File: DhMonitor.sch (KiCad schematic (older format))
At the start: 8 parts, among them J1 ProMiniDTRSide, J2 A4A5, J3 PowerRaw, J4 ProMiniRawSide, J5 RTC, J6 sdCardReader

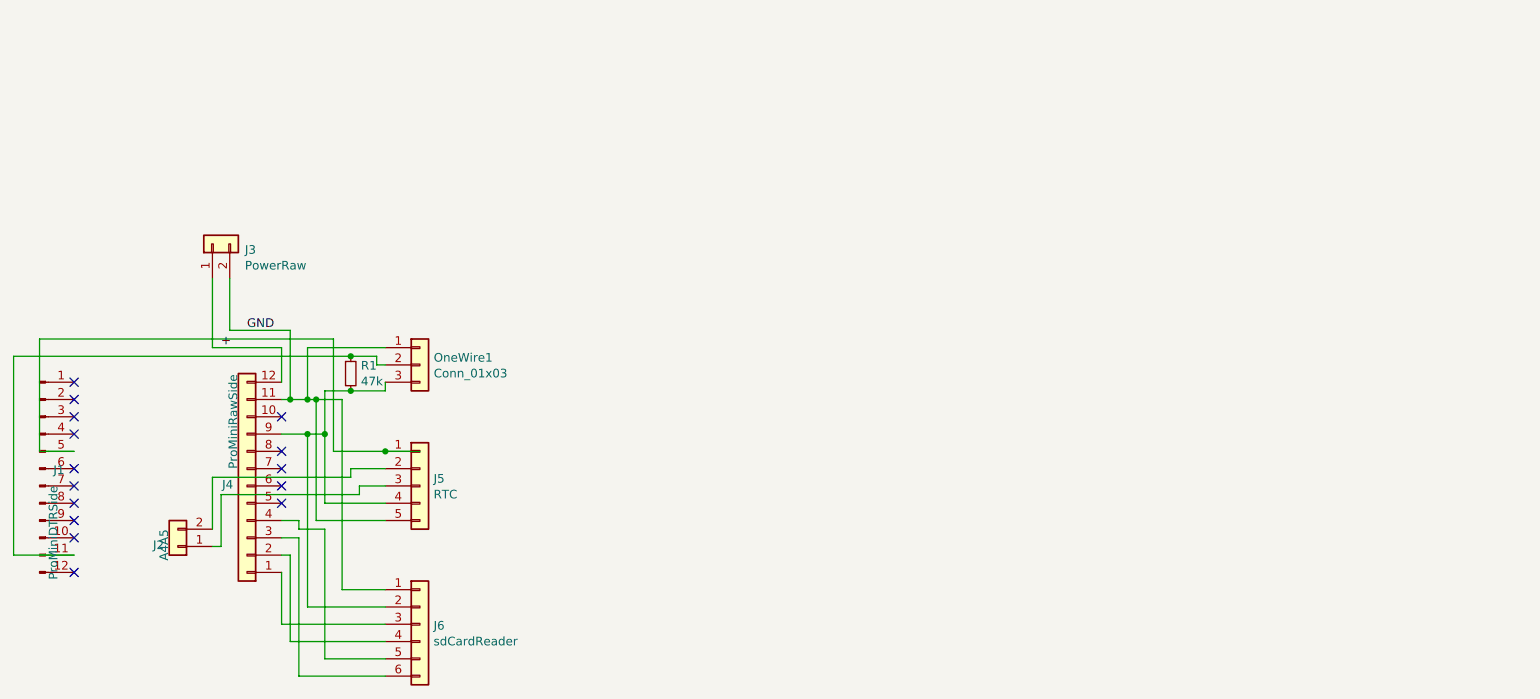
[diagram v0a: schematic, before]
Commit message: solves wrong files :o
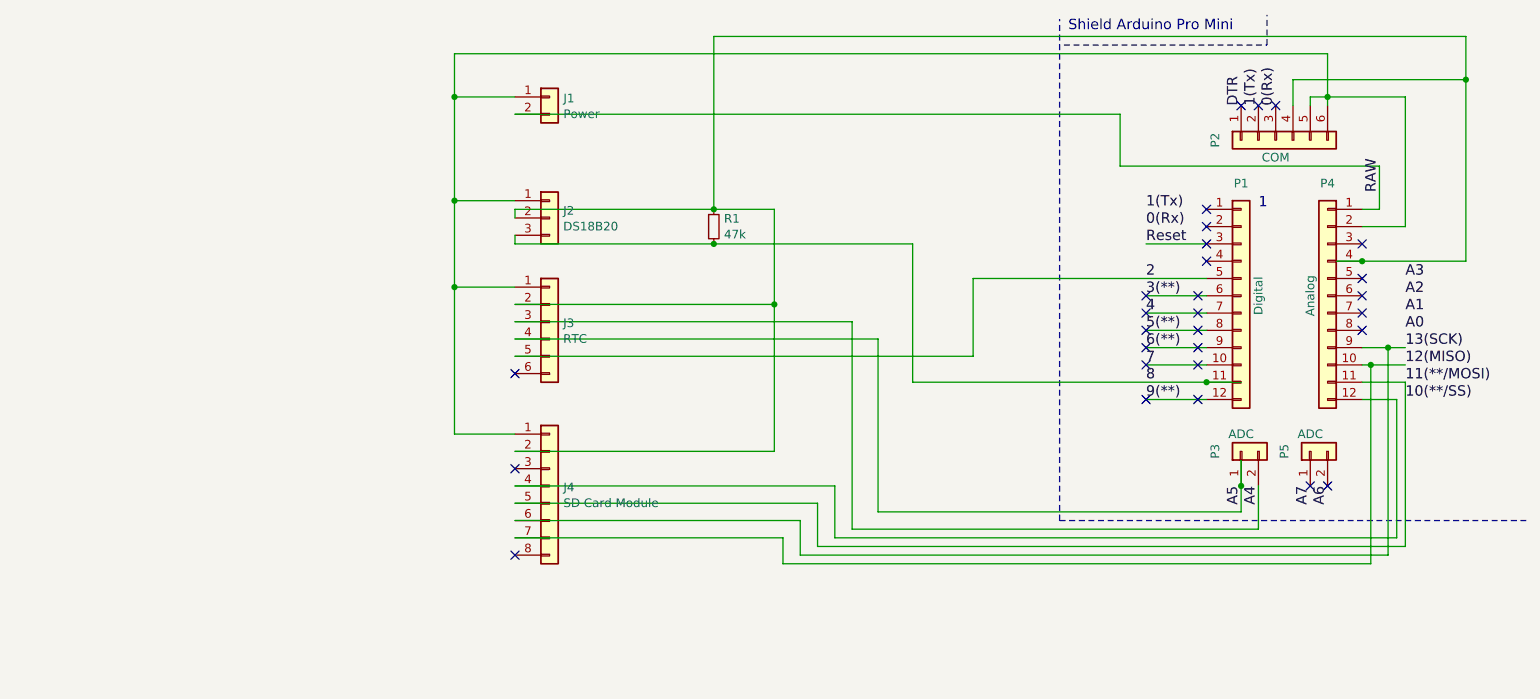
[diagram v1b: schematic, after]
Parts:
- removed J1: ProMiniDTRSide, Connector_PinSocket_2.54mm:PinSocket_1x12_P2.54mm_Vertical, symbol Connector:Conn_01x12_Male
- removed J2: A4A5, Connector_PinHeader_2.54mm:PinHeader_1x02_P2.54mm_Vertical, symbol Connector_Generic:Conn_01x02
- removed J3: PowerRaw, Connector_PinHeader_2.54mm:PinHeader_1x02_P2.54mm_Vertical, symbol Connector_Generic:Conn_01x02
- removed J4: ProMiniRawSide, Connector_PinSocket_2.54mm:PinSocket_1x12_P2.54mm_Vertical, symbol Connector_Generic:Conn_01x12
- removed J5: RTC, Connector_PinHeader_2.54mm:PinHeader_1x05_P2.54mm_Vertical, symbol Connector_Generic:Conn_01x05
- removed J6: sdCardReader, Connector_PinSocket_2.54mm:PinSocket_1x06_P2.54mm_Vertical, symbol Connector_Generic:Conn_01x06
- removed OneWire1: Conn_01x03, Connector_PinSocket_2.54mm:PinSocket_1x03_P2.54mm_Vertical, symbol Connector_Generic:Conn_01x03
- added J1: Power, Connector_PinHeader_2.54mm:PinHeader_1x02_P2.54mm_Horizontal, symbol Connector_Generic:Conn_01x02
- added J2: DS18B20, Connector_PinHeader_2.54mm:PinHeader_1x03_P2.54mm_Vertical, symbol Connector_Generic:Conn_01x03
- added J3: RTC, Connector_PinHeader_2.54mm:PinHeader_1x06_P2.54mm_Vertical, symbol Connector_Generic:Conn_01x06
- added J4: SD Card Module, Connector_PinHeader_2.54mm:PinHeader_1x08_P2.54mm_Vertical, symbol Connector_Generic:Conn_01x08
- added P1: Digital, Socket_Arduino_Pro_Mini:Socket_Strip_Arduino_1x12, symbol Connector_Generic:Conn_01x12
- added P2: COM, Socket_Arduino_Pro_Mini:Socket_Strip_Arduino_1x06, symbol Connector_Generic:Conn_01x06
- added P3, P5: ADC, Socket_Arduino_Pro_Mini:Socket_Strip_Arduino_1x02, symbol Connector_Generic:Conn_01x02
- added P4: Analog, Socket_Arduino_Pro_Mini:Socket_Strip_Arduino_1x12, symbol Connector_Generic:Conn_01x12
- R1: footprint Resistor_THT:R_Axial_DIN0204_L3.6mm_D1.6mm_P2.54mm_Vertical -> OptoDevice:R_LDR_4.9x4.2mm_P2.54mm_Vertical
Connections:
- net labels added: 0(Rx), 1(Tx), 10(**/SS), 11(**/MOSI), 12(MISO), 13(SCK), 2, 3(**), 4, 5(**), 6(**), 7, 8, 9(**), A0, A1, A2, A3, A4, A5, A6, A7, DTR, RAW, Reset
- net labels removed: +, GND
- wire segments 61 -> 83
- no-connect marks 15 -> 29
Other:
- note added: "1"
- note added: "Shield Arduino Pro Mini \n"

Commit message: v0.2: add labels + mounting holes + hx711 pinouts
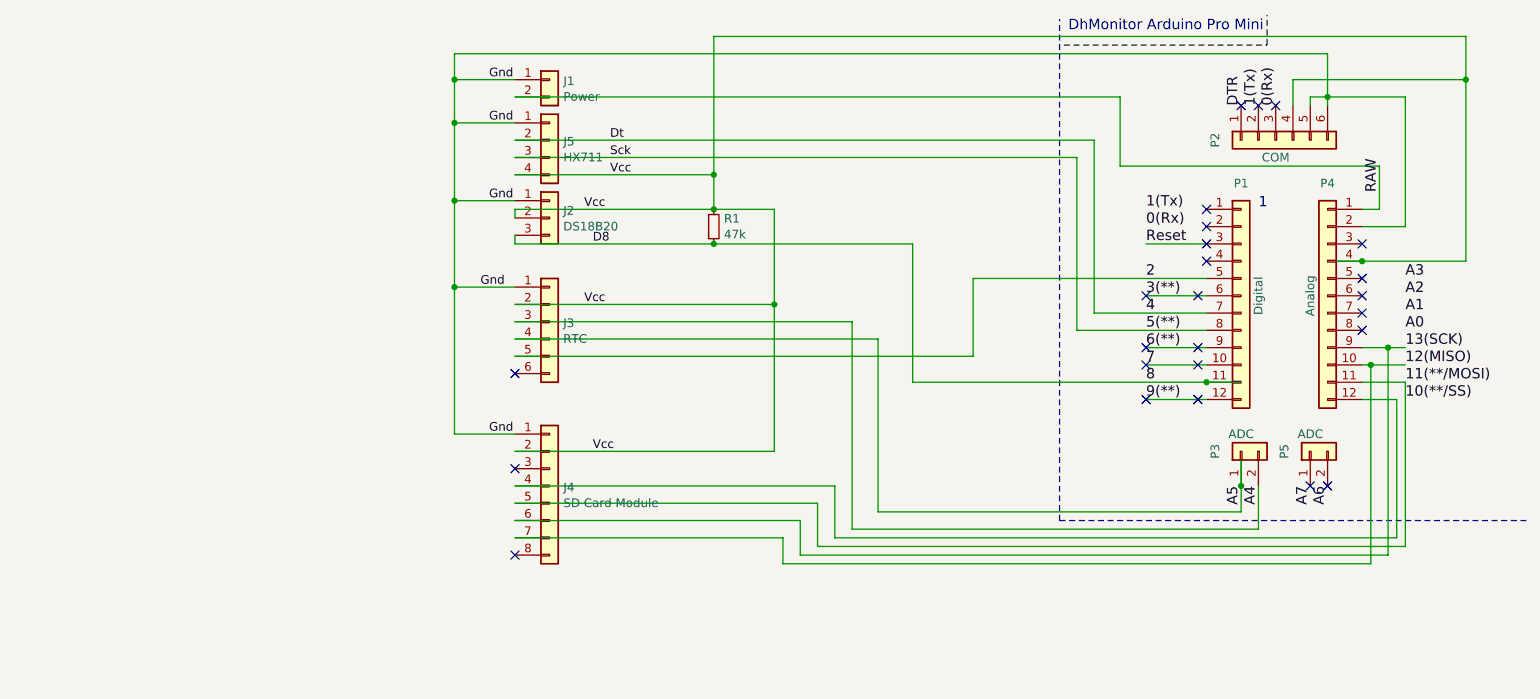
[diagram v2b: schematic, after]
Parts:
- added J5: HX711, Connector_PinHeader_2.54mm:PinHeader_1x04_P2.54mm_Vertical, symbol Connector_Generic:Conn_01x04
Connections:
- net labels added: D8, Dt, Gnd, Sck, Vcc
- wire segments 83 -> 91
- no-connect marks 29 -> 25
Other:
- note added: "DhMonitor Arduino Pro Mini \n"
- note removed: "Shield Arduino Pro Mini \n"
- moved on the sheet: J1
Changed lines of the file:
@@
 EESchema Schematic File Version 4
-LIBS:ProMini-cache
+LIBS:DhMonitor-cache
 EELAYER 26 0
 EELAYER END
@@
 encoding utf-8
 Sheet 1 1
-Title ""
+Title "DHMonitor"
 Date "sam. 04 avril 2015"
-Rev ""
+Rev "0.2"
 Comp ""
 Comment1 ""
@@
 A5
 Text Notes 8550 575  0    60   ~ 0
-Shield Arduino Pro Mini \n
+DhMonitor Arduino Pro Mini \n
 Wire Notes Line
 	8525 650  9700 650
@@
 	9350 2100 9000 2100
 Wire Wire Line
-	9350 2200 9000 2200
-Wire Wire Line
-	9000 2300 9350 2300
-Wire Wire Line
 	9350 2400 9000 2400
 Wire Wire Line
@@
 L Connector_Generic:Conn_01x02 J1
 U 1 1 5C9941D4
-P 5550 950
-F 0 "J1" H 5630 942 50  0000 L CNN
-F 1 "Power" H 5630 851 50  0000 L CNN
-F 2 "Connector_PinHeader_2.54mm:PinHeader_1x02_P2.54mm_Horizontal" H 5550 950 50  0001 C CNN
-F 3 "~" H 5550 950 50  0001 C CNN
-	1    5550 950
+P 5550 850
+F 0 "J1" H 5630 842 50  0000 L CNN
+F 1 "Power" H 5630 751 50  0000 L CNN
+F 2 "Connector_PinHeader_2.54mm:PinHeader_1x02_P2.54mm_Horizontal" H 5550 850 50  0001 C CNN
+F 3 "~" H 5550 850 50  0001 C CNN
+	1    5550 850
 	1    0    0    -1
 $EndComp
@@
 	10050 700  5000 700
 Wire Wire Line
-	5000 700  5000 950
-Wire Wire Line
-	5000 950  5350 950
-Wire Wire Line
-	5000 950  5000 1550
+	5000 850  5350 850
 Wire Wire Line
 	5000 1550 5350 1550
-Connection ~ 5000 950
 Wire Wire Line
 	5000 1550 5000 2050
@@
 	10850 600  6500 600
 Wire Wire Line
-	6500 600  6500 1600
+	6500 600  6500 1400
 Wire Wire Line
 	10100 1900 10250 1900
@@
 Connection ~ 6850 2150
 Wire Wire Line
-	5350 1050 8850 1050
-Wire Wire Line
-	8850 1050 8850 1350
+	5350 950  8850 950
 Wire Wire Line
 	8850 1350 10350 1350
@@
 	10300 2500 10500 2500
 NoConn ~ 9300 2100
-NoConn ~ 9300 2200
-NoConn ~ 9300 2300
 NoConn ~ 9300 2400
 NoConn ~ 9300 2500
 NoConn ~ 9300 2700
 NoConn ~ 9000 2100
-NoConn ~ 9000 2200
-NoConn ~ 9000 2300
 NoConn ~ 9000 2400
 NoConn ~ 9000 2500
@@
 Wire Wire Line
 	10450 2700 10250 2700
+$Comp
+L Connector_Generic:Conn_01x04 J5
+U 1 1 5C9A324B
+P 5550 1200
+F 0 "J5" H 5630 1192 50  0000 L CNN
+F 1 "HX711" H 5630 1101 50  0000 L CNN
+F 2 "Connector_PinHeader_2.54mm:PinHeader_1x04_P2.54mm_Vertical" H 5550 1200 50  0001 C CNN
+F 3 "~" H 5550 1200 50  0001 C CNN
+	1    5550 1200
+	1    0    0    -1
+$EndComp
+Wire Wire Line
+	8700 2200 8700 1200
+Wire Wire Line
+	8700 2200 9350 2200
+Wire Wire Line
+	8600 2300 8600 1300
+Wire Wire Line
+	8600 2300 9350 2300
+Text Label 5750 1600 0    50   ~ 0
+Vcc
+Text Label 5750 2150 0    50   ~ 0
+Vcc
+Text Label 5800 3000 0    50   ~ 0
+Vcc
+Text Label 5800 1800 0    50   ~ 0
+D8
+Text Label 5150 2050 0    50   ~ 0
+Gnd
+Text Label 5200 1550 0    50   ~ 0
+Gnd
+Wire Wire Line
+	5000 700  5000 850
+Connection ~ 5000 850
+Wire Wire Line
+	5000 850  5000 1100
+Wire Wire Line
+	8850 950  8850 1350
+Wire Wire Line
+	5350 1100 5000 1100
+Connection ~ 5000 1100
+Wire Wire Line
+	5000 1100 5000 1550
+Wire Wire Line
+	8700 1200 5350 1200
+Wire Wire Line
+	8600 1300 5350 1300
+Wire Wire Line
+	5350 1400 6500 1400
+Connection ~ 6500 1400
+Wire Wire Line
+	6500 1400 6500 1600
+Text Label 5200 1100 0    50   ~ 0
+Gnd
+Text Label 5200 2900 0    50   ~ 0
+Gnd
+Text Label 5200 850  0    50   ~ 0
+Gnd
+Text Label 5900 1400 0    50   ~ 0
+Vcc
+Text Label 5900 1300 0    50   ~ 0
+Sck
+Text Label 5900 1200 0    50   ~ 0
+Dt
 $EndSCHEMATC
